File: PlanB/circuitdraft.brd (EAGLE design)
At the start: 24 x 43 mm, 20 parts, among them Q1 16 MHz

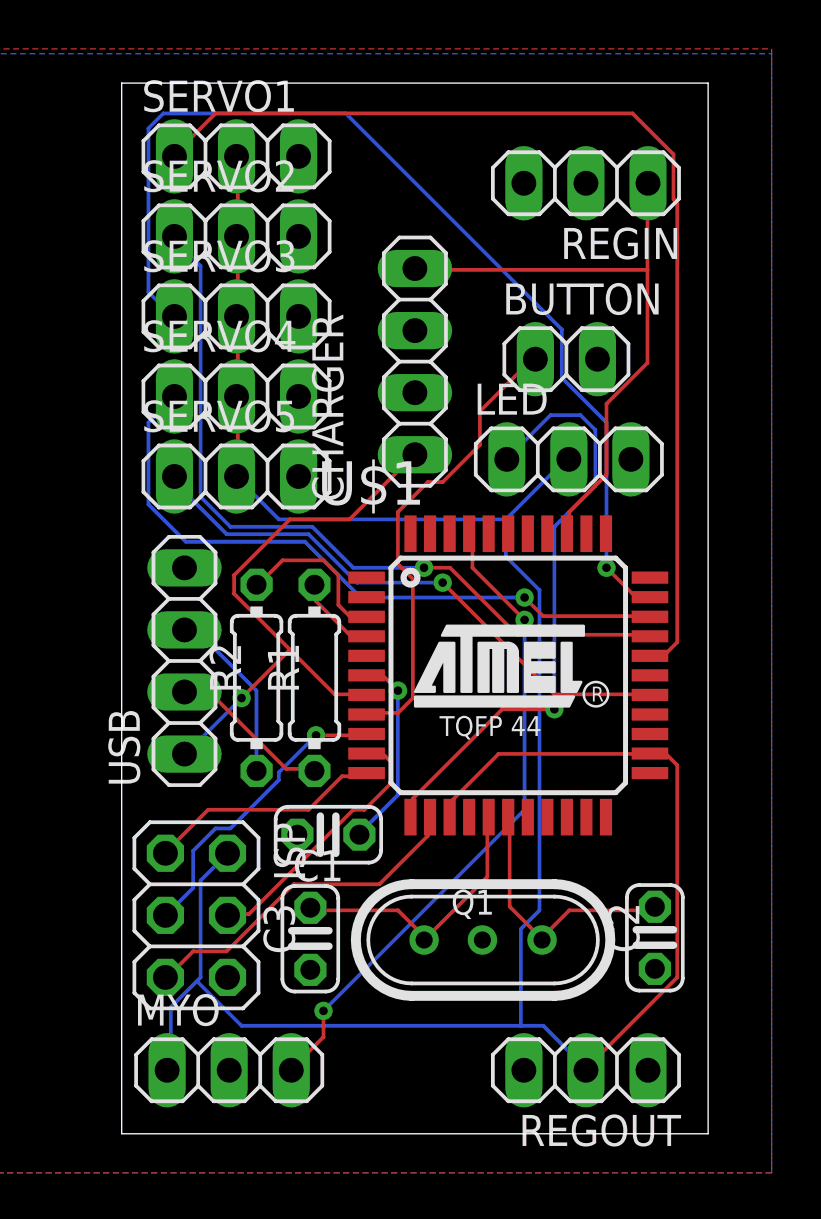
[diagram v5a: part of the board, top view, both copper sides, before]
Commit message: shifted regulator to ensure enough spacing between daughterboards
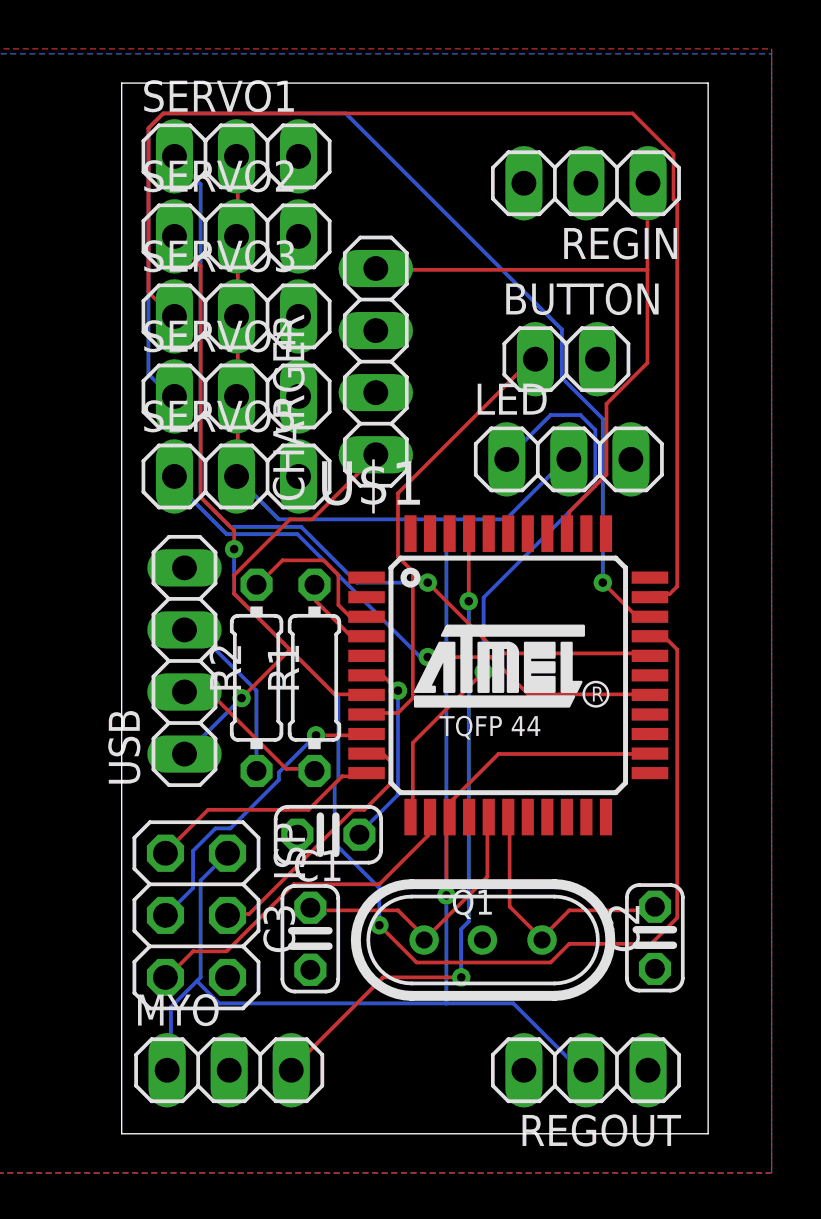
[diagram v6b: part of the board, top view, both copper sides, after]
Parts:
- moved CHARGER 1.60 mm to (15.4, 31.6)
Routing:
- net SIGNAL2: track 31.8 -> 57.7 mm, vias 1 -> 2
- net SIGNAL4: track 27.3 -> 45.9 mm
- net POWER: track 102.5 -> 88.8 mm, vias 0 -> 1
- net SIGNAL3: track 41.8 -> 49.7 mm, vias 1 -> 0
- net SIGNAL1: track 43.3 -> 35.5 mm, vias 0 -> 1
- net VBAT: track 25.2 -> 26.8 mm
- net VBUS: track 23.4 -> 21.8 mm
- net DATAIN: track 24.8 -> 23.6 mm
